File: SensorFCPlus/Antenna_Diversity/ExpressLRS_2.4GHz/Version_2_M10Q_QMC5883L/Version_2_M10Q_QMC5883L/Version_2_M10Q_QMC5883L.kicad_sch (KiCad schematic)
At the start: 7 parts, among them U1 QMC5883L

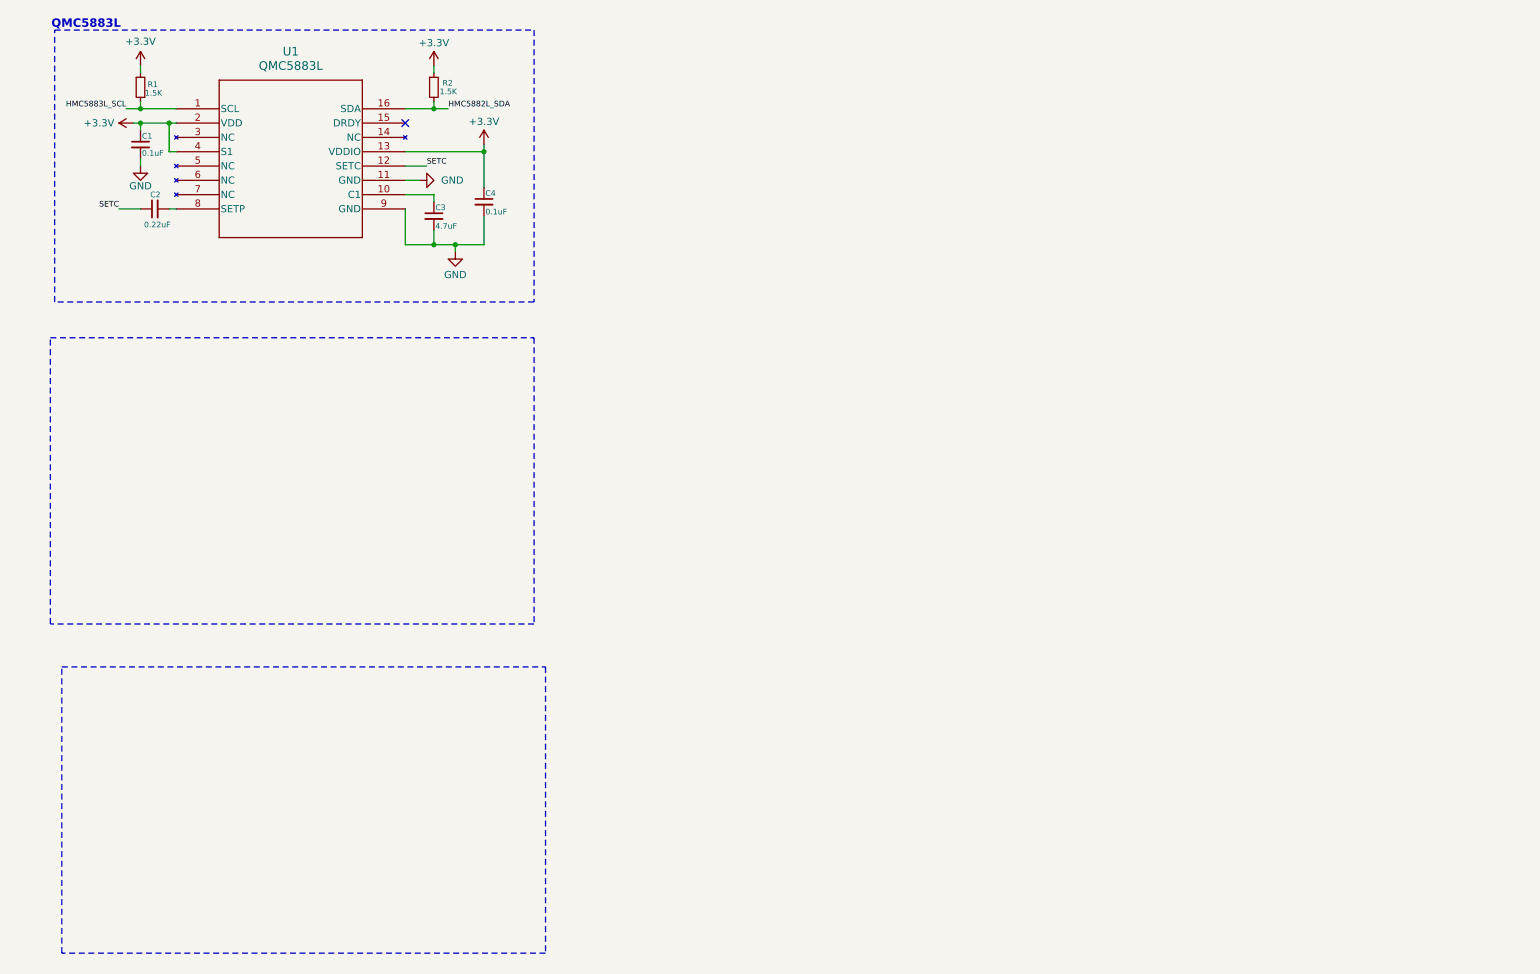
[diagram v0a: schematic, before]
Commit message: Update KiCad schematic and project files for ExpressLRS 2.4GHz modules (Version 1 and 2) and add new components (ESP8285, SE2431L, SX1280)
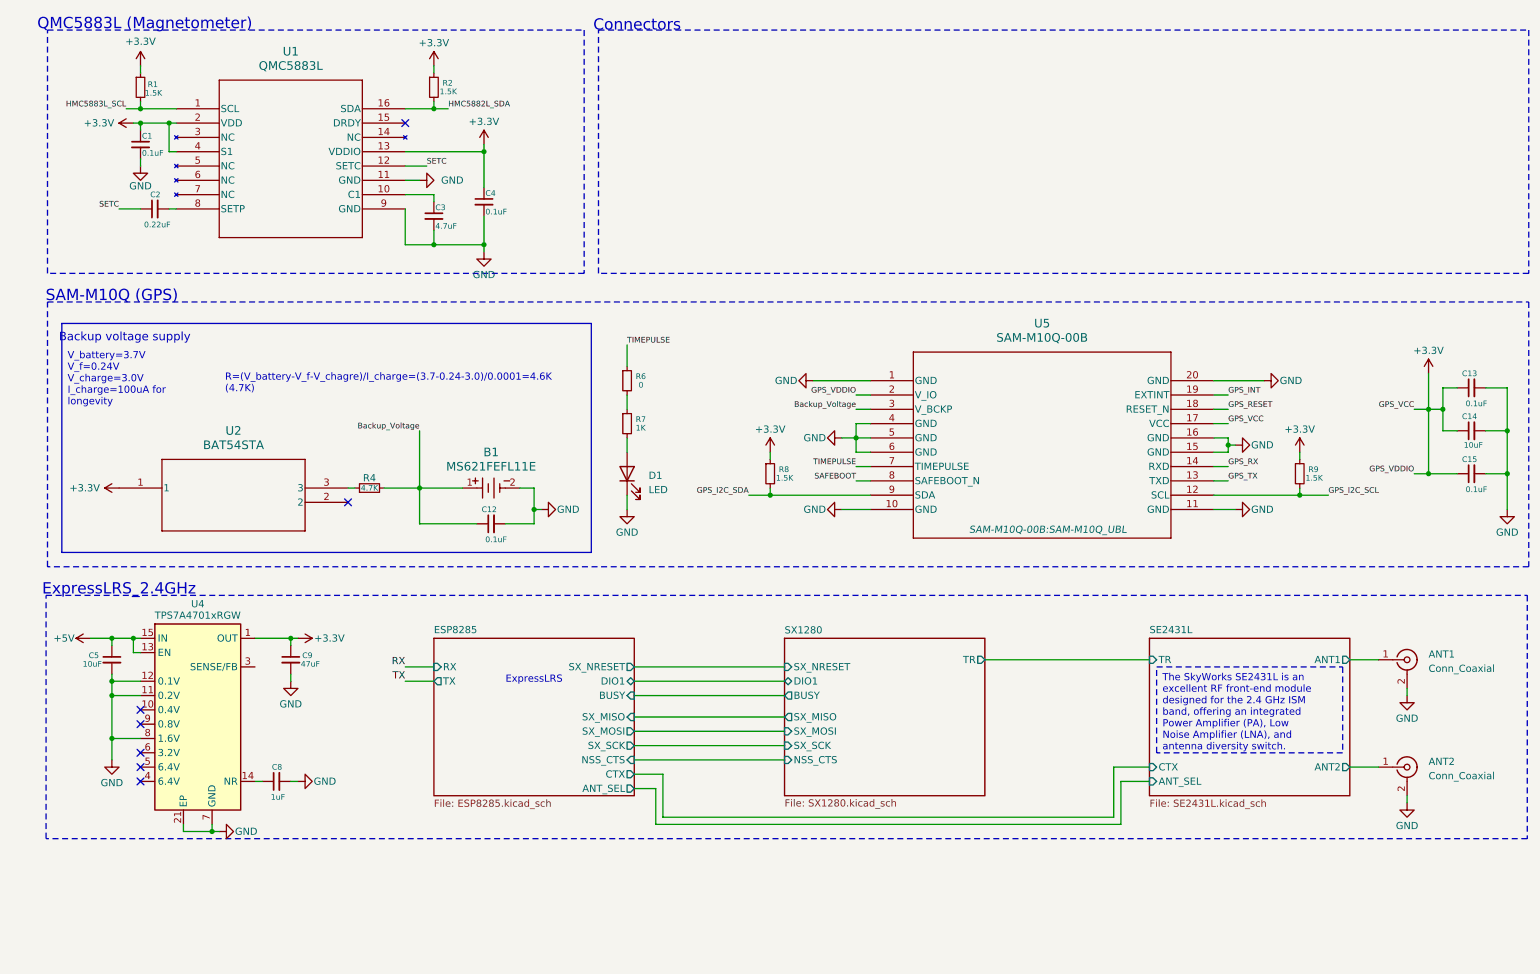
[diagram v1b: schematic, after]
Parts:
- added ANT1, ANT2: Conn_Coaxial, Connector_Coaxial:U.FL_Hirose_U.FL-R-SMT-1_Vertical, symbol Connector:Conn_Coaxial
- added B1: MS621FEFL11E, MS621FE-FL11E:MS621FE-FL11E, symbol MS621FE-FL11E:MS621FEFL11E
- added C12, C13, C15: 0.1uF, Capacitor_SMD:C_0805_2012Metric_Pad1.18x1.45mm_HandSolder, symbol Device:C_Small
- added C14: 10uF, ECASD40J106M055K00:ECASD40J106M055K00, symbol Device:C_Small
- added C5: 10uF, Capacitor_SMD:C_0805_2012Metric_Pad1.18x1.45mm_HandSolder, symbol Device:C_Small
- added C8: 1uF, Capacitor_SMD:C_0805_2012Metric_Pad1.18x1.45mm_HandSolder, symbol Device:C_Small
- added C9: 47uF, Capacitor_SMD:C_0805_2012Metric_Pad1.18x1.45mm_HandSolder, symbol Device:C_Small
- added D1: LED, LED_SMD:LED_0805_2012Metric_Pad1.15x1.40mm_HandSolder, symbol Device:LED
- added R4: 4.7K, Resistor_SMD:R_0805_2012Metric_Pad1.20x1.40mm_HandSolder, symbol Device:R_Small
- added R6: 0, Resistor_SMD:R_0805_2012Metric_Pad1.20x1.40mm_HandSolder, symbol Device:R_Small
- added R7: 1K, Resistor_SMD:R_0805_2012Metric_Pad1.20x1.40mm_HandSolder, symbol Device:R_Small
- added R8, R9: 1.5K, Resistor_SMD:R_0805_2012Metric_Pad1.20x1.40mm_HandSolder, symbol Device:R_Small
- added U2: BAT54STA, SOT23_BAT54STA_1P7XP85_DIO, symbol BAT54STA:BAT54STA
- added U4: TPS7A4701xRGW, Package_DFN_QFN:Texas_RGW0020A_VQFN-20-1EP_5x5mm_P0.65mm_EP3.15x3.15mm_ThermalVias, symbol Regulator_Linear:TPS7A4701xRGW
- added U5: SAM-M10Q-00B, SAM-M10Q-00B:SAM-M10Q_UBL, symbol SAM-M10Q-00B:SAM-M10Q-00B
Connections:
- net +3.3V: now also C13.1, C14.1, C15.1, C9.1, R8.1, R9.1, U2.1, U4.1 (OUT), U4.20 (OUT), U5.17 (VCC), U5.2 (V_IO)
- net GND: now also ANT1.2 (Ext), ANT2.2 (Ext), B1.2, C12.2, C13.2, C14.2, C15.2, C5.2, C8.2, C9.2, D1.1 (K), U4.11 (0.2V), U4.12 (0.1V), U4.21 (EP), U4.7 (GND), U4.8 (1.6V), U5.1 (GND), U5.10 (GND), U5.11 (GND), U5.15 (GND), U5.16 (GND), U5.20 (GND), U5.4 (GND), U5.5 (GND), U5.6 (GND)
- new net: R4.1, U2.3
- new net: R6.2, R7.1
- new net: C8.1, U4.14 (NR)
- new net: D1.2 (A), R7.2
- new net +5V: C5.1, U4.13 (EN), U4.15 (IN), U4.16 (IN)
- new net Backup_Voltage: B1.1, C12.1, R4.2, U5.3 (V_BCKP)
- new net GPS_I2C_SCL: R9.2, U5.12 (SCL)
- new net GPS_I2C_SDA: R8.2, U5.9 (SDA)
- new net GPS_INT: U5.19 (EXTINT)
- new net GPS_RESET: U5.18 (RESET_N)
- new net GPS_RX: U5.14 (RXD)
- new net GPS_TX: U5.13 (TXD)
- new net SAFEBOOT: U5.8 (SAFEBOOT_N)
- new net SE2431L/ANT1: ANT1.1 (In)
- new net SE2431L/ANT2: ANT2.1 (In)
- new net TIMEPULSE: R6.1, U5.7 (TIMEPULSE)
- no-connect marks 1 -> 7
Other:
- added sheet ESP8285 (ESP8285.kicad_sch)
- added sheet SE2431L (SE2431L.kicad_sch)
- added sheet SX1280 (SX1280.kicad_sch)
- note added: "Backup voltage supply"
- note added: "Connectors"
- note added: "ExpressLRS"
- note added: "ExpressLRS_2.4GHz"
- note added: "QMC5883L (Magnetometer)"
- note added: "SAM-M10Q (GPS)"
- note removed: "QMC5883L"

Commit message: Update README.md and Version 2 files; add new GIF and MP4 for Version 2
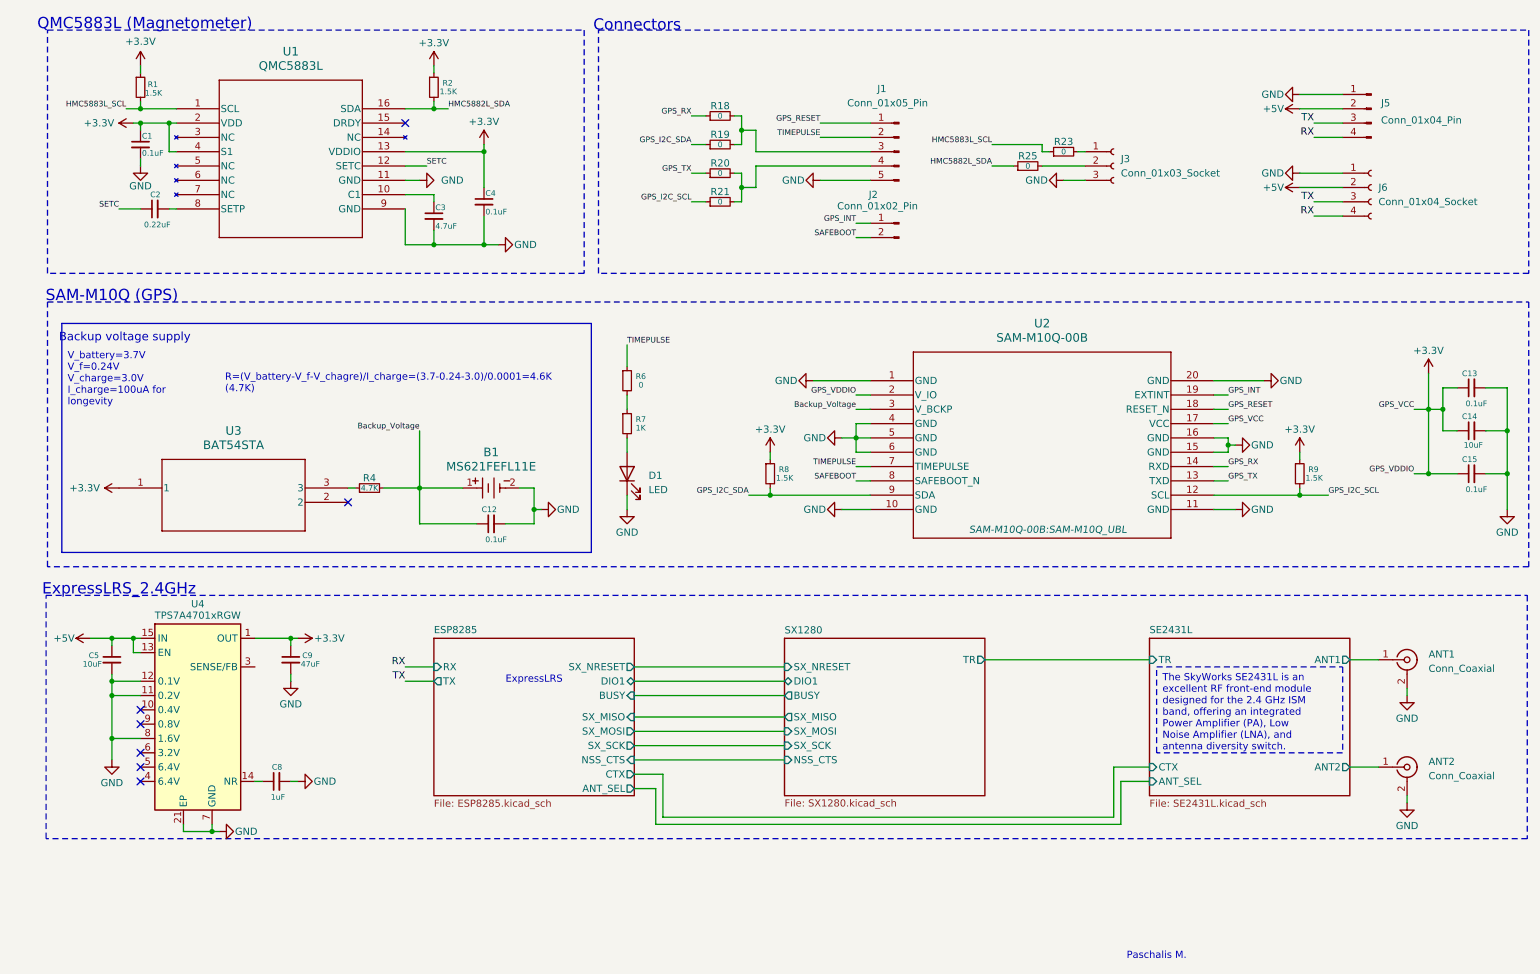
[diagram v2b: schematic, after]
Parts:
- added J1: Conn_01x05_Pin, Connector_PinHeader_2.00mm:PinHeader_1x05_P2.00mm_Vertical, symbol Connector:Conn_01x05_Pin
- added J2: Conn_01x02_Pin, Connector_PinHeader_2.00mm:PinHeader_1x02_P2.00mm_Vertical, symbol Connector:Conn_01x02_Pin
- added J3: Conn_01x03_Socket, Connector_JST:JST_GH_SM03B-GHS-TB_1x03-1MP_P1.25mm_Horizontal, symbol Connector:Conn_01x03_Socket
- added J5: Conn_01x04_Pin, Connector_JST:JST_GH_SM04B-GHS-TB_1x04-1MP_P1.25mm_Horizontal, symbol Connector:Conn_01x04_Pin
- added J6: Conn_01x04_Socket, Connector_Harwin:Harwin_M20-89004xx_1x04_P2.54mm_Horizontal, symbol Connector:Conn_01x04_Socket
- added R18, R19, R20, R21, R23, R25: 0, Resistor_SMD:R_0603_1608Metric_Pad0.98x0.95mm_HandSolder, symbol Device:R_Small
- U3: renamed from U2; footprint SOT23_BAT54STA_1P7XP85_DIO -> BAT54STA:BAT54STA
- renumbered U5 to U2
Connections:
- net +5V: now also J5.2 (Pin_2), J6.2 (Pin_2)
- net GND: now also J1.5 (Pin_5), J3.3 (Pin_3), J5.1 (Pin_1), J6.1 (Pin_1)
- net GPS_I2C_SCL: now also R21.1
- net GPS_I2C_SDA: now also R19.1
- net GPS_INT: now also J2.1 (Pin_1)
- net GPS_RESET: now also J1.1 (Pin_1)
- net GPS_RX: now also R18.1
- net GPS_TX: now also R20.1
- net HMC5882L_SDA: now also R25.1
- net HMC5883L_SCL: now also R23.1
- net RX: now also J5.4 (Pin_4), J6.4 (Pin_4)
- net SAFEBOOT: now also J2.2 (Pin_2)
- net TIMEPULSE: now also J1.2 (Pin_2)
- net TX: now also J5.3 (Pin_3), J6.3 (Pin_3)
- new net: J1.3 (Pin_3), R18.2, R19.2
- new net: J1.4 (Pin_4), R20.2, R21.2
- new net: J3.2 (Pin_2), R25.2
- new net: J3.1 (Pin_1), R23.2
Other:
- note added: "Paschalis M."
- company: (none) -> https://github.com/Paschalis
- title: (none) -> Version 2 (GPS:M10Q, MAG:QMC5883L, ELRS:2.4GHz_RX)
